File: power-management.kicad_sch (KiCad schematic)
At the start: 11 parts, among them Q3 DMP2070UQ-7, U2 AP2112K-3.3

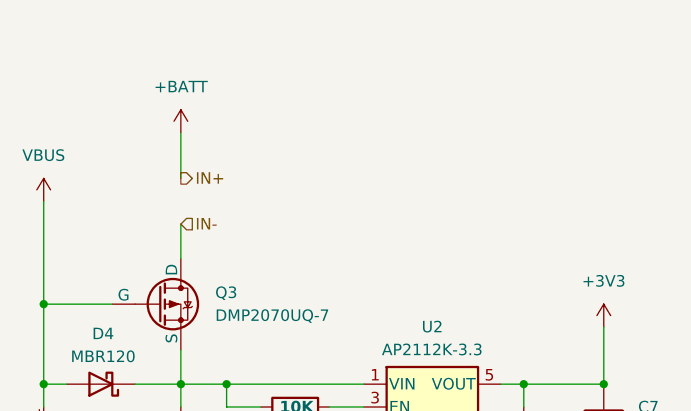
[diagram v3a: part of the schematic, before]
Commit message: Adding more 0 ohm resistors and pullups for I2C lines
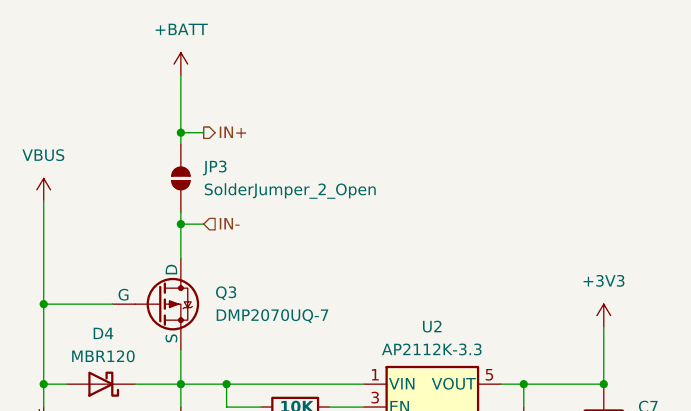
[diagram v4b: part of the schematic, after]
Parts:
- added JP3: SolderJumper_2_Open, Jumper:SolderJumper-2_P1.3mm_Open_TrianglePad1.0x1.5mm, symbol Jumper:SolderJumper_2_Open
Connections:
- net +BATT: now also JP3.2 (B)
- net IN-: now also JP3.1 (A)
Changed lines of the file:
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@@
+	)
+	(junction
+		(at 96.52 87.63)
+		(diameter 0)
+		(color 0 0 0 0)
 	)
 	(junction
@@
 	)
 	(junction
+		(at 96.52 77.47)
+		(diameter 0)
+		(color 0 0 0 0)
+	)
+	(junction
 		(at 134.62 105.41)
 		(diameter 0)
@@
 	(wire
 		(pts
+			(xy 96.52 86.36) (xy 96.52 87.63)
+		)
+		(stroke
+			(width 0)
+			(type default)
+		)
+	)
+	(wire
+		(pts
+			(xy 99.06 87.63) (xy 96.52 87.63)
+		)
+		(stroke
+			(width 0)
+			(type default)
+		)
+	)
+	(wire
+		(pts
 			(xy 143.51 113.03) (xy 143.51 115.57)
 		)
@@
 	(wire
 		(pts
-			(xy 96.52 77.47) (xy 96.52 82.55)
-		)
-		(stroke
-			(width 0)
-			(type default)
-		)
-	)
-	(wire
-		(pts
 			(xy 134.62 105.41) (xy 143.51 105.41)
 		)
@@
 	(wire
 		(pts
+			(xy 96.52 87.63) (xy 96.52 91.44)
+		)
+		(stroke
+			(width 0)
+			(type default)
+		)
+	)
+	(wire
+		(pts
 			(xy 91.44 105.41) (xy 96.52 105.41)
 		)
@@
 	(wire
 		(pts
+			(xy 99.06 77.47) (xy 96.52 77.47)
+		)
+		(stroke
+			(width 0)
+			(type default)
+		)
+	)
+	(wire
+		(pts
 			(xy 163.83 99.06) (xy 163.83 105.41)
 		)
@@
 	(wire
 		(pts
+			(xy 96.52 77.47) (xy 96.52 71.12)
+		)
+		(stroke
+			(width 0)
+			(type default)
+		)
+	)
+	(wire
+		(pts
 			(xy 113.03 107.95) (xy 116.84 107.95)
 		)
@@
 	(wire
 		(pts
+			(xy 96.52 77.47) (xy 96.52 78.74)
+		)
+		(stroke
+			(width 0)
+			(type default)
+		)
+	)
+	(wire
+		(pts
 			(xy 134.62 107.95) (xy 134.62 105.41)
-		)
-		(stroke
-			(width 0)
-			(type default)
-		)
-	)
-	(wire
-		(pts
-			(xy 96.52 87.63) (xy 96.52 91.44)
 		)
 		(stroke
@@
 	(hierarchical_label "IN+"
 		(shape output)
-		(at 96.52 82.55 0)
+		(at 99.06 77.47 0)
 		(fields_autoplaced yes)
 		(effects
@@
 	(hierarchical_label "IN-"
 		(shape input)
-		(at 96.52 87.63 0)
+		(at 99.06 87.63 0)
 		(fields_autoplaced yes)
 		(effects
@@
 	)
 	(symbol
+		(lib_id "Jumper:SolderJumper_2_Open")
+		(at 96.52 82.55 90)
+		(unit 1)
+		(exclude_from_sim yes)
+		(in_bom no)
+		(on_board yes)
+		(dnp no)
+		(property "Reference" "JP3"
+			(at 99.06 81.2799 90)
+			(effects
+				(font
+					(size 1.27 1.27)
+				)
+				(justify right)
+			)
+		)
+		(property "Value" "SolderJumper_2_Open"
+			(at 99.06 83.8199 90)
+			(effects
+				(font
+					(size 1.27 1.27)
+				)
+				(justify right)
+			)
+		)
+		(property "Footprint" "Jumper:SolderJumper-2_P1.3mm_Open_TrianglePad1.0x1.5mm"
+			(at 96.52 82.55 0)
+			(effects
+				(font
+					(size 1.27 1.27)
+				)
+				(hide yes)
+			)
+		)
+		(property "Datasheet" "~"
+			(at 96.52 82.55 0)
+			(effects
+				(font
+					(size 1.27 1.27)
+				)
+				(hide yes)
+			)
+		)
+		(property "Description" "Solder Jumper, 2-pole, open"
+			(at 96.52 82.55 0)
+			(effects
+				(font
+					(size 1.27 1.27)
+				)
+				(hide yes)
+			)
+		)
+		(property "Mfr" ""
+			(at 96.52 82.55 0)
+			(effects
+				(font
+					(size 1.27 1.27)
+				)
+				(hide yes)
+			)
+		)
+		(property "Mfr P/N" ""
+			(at 96.52 82.55 0)
+			(effects
+				(font
+					(size 1.27 1.27)
+				)
+				(hide yes)
+			)
+		)
+		(property "Supplier_1" ""
+			(at 96.52 82.55 0)
+			(effects
+				(font
+					(size 1.27 1.27)
+				)
+				(hide yes)
+			)
+		)
+		(property "Supplier_1 P/N" ""
+			(at 96.52 82.55 0)
+			(effects
+				(font
+					(size 1.27 1.27)
+				)
+				(hide yes)
+			)
+		)
+		(property "Supplier_1 Unit Price" ""
+			(at 96.52 82.55 0)
+			(effects
+				(font
+					(size 1.27 1.27)
+				)
+				(hide yes)
+			)
+		)
+		(property "Supplier_1 Price @ Qty" ""
+			(at 96.52 82.55 0)
+			(effects
+				(font
+					(size 1.27 1.27)
+				)
+				(hide yes)
+			)
+		)
+		(property "Supplier_2" ""
+			(at 96.52 82.55 0)
+			(effects
+				(font
+					(size 1.27 1.27)
+				)
+				(hide yes)
+			)
+		)
+		(property "Supplier_2 P/N" ""
+			(at 96.52 82.55 0)
+			(effects
+				(font
+					(size 1.27 1.27)
+				)
+				(hide yes)
+			)
+		)
+		(property "Supplier_2 Unit Price" ""
+			(at 96.52 82.55 0)
+			(effects
+				(font
+					(size 1.27 1.27)
+				)
+				(hide yes)
+			)
+		)
+		(property "Supplier_2 Price @ Qty" ""
+			(at 96.52 82.55 0)
+			(effects
+				(font
+					(size 1.27 1.27)
+				)
+				(hide yes)
+			)
+		)
+		(pin "1"
+		)
+		(pin "2"
+		)
+		(instances
+			(project "roamer"
+				(path "/1c59de6a-87fe-4223-8898-4b0383164a31/f8947920-db82-4e9f-9d4f-25a180fcfca7"
+					(reference "JP3")
+					(unit 1)
+				)
+			)
+		)
+	)
+	(symbol
 		(lib_id "power:+BATT")
-		(at 96.52 77.47 0)
+		(at 96.52 71.12 0)
 		(unit 1)
 		(exclude_from_sim no)
@@
 		(fields_autoplaced yes)
 		(property "Reference" "#PWR020"
-			(at 96.52 81.28 0)
+			(at 96.52 74.93 0)
 			(effects
 				(font
@@
 		)
 		(property "Value" "+BATT"
-			(at 96.52 72.39 0)
+			(at 96.52 66.04 0)
 			(effects
 				(font
@@
 		)
 		(property "Footprint" ""
-			(at 96.52 77.47 0)
+			(at 96.52 71.12 0)
 			(effects
 				(font
@@
 		)
 		(property "Datasheet" ""
-			(at 96.52 77.47 0)
+			(at 96.52 71.12 0)
 			(effects
 				(font
@@
 		)
 		(property "Description" "Power symbol creates a global label with name \"+BATT\""
-			(at 96.52 77.47 0)
-			(effects
-				(font
+			(at 96.52 71.12 0)
+			(effects
+				(font

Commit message: Adding testpoints to I2C, SPI, and signals
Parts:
- added TP7: TestPoint, TestPoint:TestPoint_Loop_D2.50mm_Drill1.0mm, symbol Connector:TestPoint
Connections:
- net +3V3: now also TP7.1
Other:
- moved on the sheet: C10, C11, C5

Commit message: Fixing lots of ERC errors
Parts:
- removed R9: 100K, Resistor_SMD:R_Array_Convex_4x1206, symbol Device:R_Network04_Split
- added R9: 100K, Resistor_THT:R_Array_SIP8, symbol Device:R_Pack04_SIP_Split
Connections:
- net GND: now also R9.5 (R3.1)
- net VBUS: now also R9.6 (R3.2)
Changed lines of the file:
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@@
+	)
+	(junction
+		(at 109.22 105.41)
+		(diameter 0)
+		(color 0 0 0 0)
 	)
 	(junction
@@
 	(wire
 		(pts
-			(xy 101.6 105.41) (xy 116.84 105.41)
+			(xy 101.6 105.41) (xy 109.22 105.41)
 		)
 		(stroke
@@
 		(pts
 			(xy 96.52 105.41) (xy 96.52 107.95)
+		)
+		(stroke
+			(width 0)
+			(type default)
+		)
+	)
+	(wire
+		(pts
+			(xy 109.22 105.41) (xy 116.84 105.41)
 		)
 		(stroke
@@
 	)
 	(symbol
+		(lib_id "power:PWR_FLAG")
+		(at 109.22 105.41 0)
+		(unit 1)
+		(exclude_from_sim no)
+		(in_bom yes)
+		(on_board yes)
+		(dnp no)
+		(property "Reference" "#FLG05"
+			(at 109.22 103.505 0)
+			(effects
+				(font
+					(size 1.27 1.27)
+				)
+				(hide yes)
+			)
+		)
+		(property "Value" "PWR_FLAG"
+			(at 109.474 101.854 0)
+			(effects
+				(font
+					(size 1.27 1.27)
+				)
+			)
+		)
+		(property "Footprint" ""
+			(at 109.22 105.41 0)
+			(effects
+				(font
+					(size 1.27 1.27)
+				)
+				(hide yes)
+			)
+		)
+		(property "Datasheet" "~"
+			(at 109.22 105.41 0)
+			(effects
+				(font
+					(size 1.27 1.27)
+				)
+				(hide yes)
+			)
+		)
+		(property "Description" "Special symbol for telling ERC where power comes from"
+			(at 109.22 105.41 0)
+			(effects
+				(font
+					(size 1.27 1.27)
+				)
+				(hide yes)
+			)
+		)
+		(pin "1"
+		)
+		(instances
+			(project ""
+				(path "/1c59de6a-87fe-4223-8898-4b0383164a31/f8947920-db82-4e9f-9d4f-25a180fcfca7"
+					(reference "#FLG05")
+					(unit 1)
+				)
+			)
+		)
+	)
+	(symbol
 		(lib_id "Device:C")
 		(at 143.51 109.22 0)
@@
 					(reference "C7")
 					(unit 1)
-				)
-			)
-		)
-	)
-	(symbol
-		(lib_id "Device:R_Network04_Split")
-		(at 81.28 111.76 0)
-		(unit 3)
-		(exclude_from_sim no)
-		(in_bom yes)
-		(on_board yes)
-		(dnp no)
-		(property "Reference" "R9"
-			(at 83.82 110.4899 0)
-			(effects
-				(font
-					(size 1.27 1.27)
-				)
-				(justify left)
-			)
-		)
-		(property "Value" "100K"
-			(at 81.534 114.3 90)
-			(effects
-				(font
-					(size 1.27 1.27)
-					(thickness 0.254)
-					(bold yes)
-				)
-				(justify left)
-			)
-		)
-		(property "Footprint" "Resistor_SMD:R_Array_Convex_4x1206"
-			(at 79.248 111.76 90)
-			(effects
-				(font
-					(size 1.27 1.27)
-				)
-				(hide yes)
-			)
-		)
-		(property "Datasheet" "https://www.bourns.com/docs/Product-Datasheets/CATCAY.pdf"
-			(at 81.28 111.76 0)
-			(effects
-				(font
-					(size 1.27 1.27)
-				)
-				(hide yes)
-			)
-		)
-		(property "Description" "100k Ohm 1% 62.5mW Power Per Element Isolated 4 Resistor Network/Array 200pm/°C 1206 (3216 Metric), Convex, Long Side Terminals."
-			(at 81.28 111.76 0)
-			(effects
-				(font
-					(size 1.27 1.27)
-				)
-				(hide yes)
-			)
-		)
-		(property "Mfr" "Bourns Inc."
-			(at 81.28 111.76 0)
-			(effects
-				(font
-					(size 1.27 1.27)
-				)
-				(hide yes)
-			)
-		)
-		(property "Mfr P/N" "CAY16-1003F4LF"
-			(at 81.28 111.76 0)
-			(effects
-				(font
-					(size 1.27 1.27)
-				)
-				(hide yes)
-			)
-		)
-		(property "Supplier_1" "Digikey"
-			(at 81.28 111.76 0)
-			(effects
-				(font
-					(size 1.27 1.27)
-				)
-				(hide yes)
-			)
-		)
-		(property "Supplier_1 P/N" "CAY16-1003F4LFCT-ND"
-			(at 81.28 111.76 0)
-			(effects
-				(font
-					(size 1.27 1.27)
-				)
-				(hide yes)
-			)
-		)
-		(property "Supplier_1 Unit Price" "0.10"
-			(at 81.28 111.76 0)
-			(effects
-				(font
-					(size 1.27 1.27)
-				)
-				(hide yes)
-			)
-		)
-		(property "Supplier_1 Price @ Qty" "0.03170"
-			(at 81.28 111.76 0)
-			(effects
-				(font
-					(size 1.27 1.27)
-				)
-				(hide yes)
-			)
-		)
-		(property "Supplier_2" ""
-			(at 81.28 111.76 0)
-			(effects
-				(font
-					(size 1.27 1.27)
-				)
-				(hide yes)
-			)
-		)
-		(property "Supplier_2 P/N" ""
-			(at 81.28 111.76 0)
-			(effects
-				(font
-					(size 1.27 1.27)
-				)
-				(hide yes)
-			)
-		)
-		(property "Supplier_2 Unit Price" ""
-			(at 81.28 111.76 0)
-			(effects
-				(font
-					(size 1.27 1.27)
-				)
-				(hide yes)
-			)
-		)
-		(property "Supplier_2 Price @ Qty" ""
-			(at 81.28 111.76 0)
-			(effects
-				(font
-					(size 1.27 1.27)
-				)
-				(hide yes)
-			)
-		)
-		(pin "2"
-		)
-		(pin "3"
-		)
-		(pin "4"
-		)
-		(pin "5"
-		)
-		(pin "1"
-		)
-		(instances
-			(project "roamer"
-				(path "/1c59de6a-87fe-4223-8898-4b0383164a31/f8947920-db82-4e9f-9d4f-25a180fcfca7"
-					(reference "R9")
-					(unit 3)
 				)
 			)
@@
 				)
 			)
+		)
+	)
+	(symbol
+		(lib_id "Device:R_Pack04_SIP_Split")
+		(at 81.28 111.76 0)
+		(unit 3)
+		(exclude_from_sim no)
+		(in_bom yes)
+		(on_board yes)
+		(dnp no)
+		(property "Reference" "R9"
+			(at 83.82 110.4899 0)
+			(effects
+				(font
+					(size 1.27 1.27)
+				)
+				(justify left)
+			)
+		)
+		(property "Value" "100K"
+			(at 81.28 114.554 90)
+			(effects
+				(font
+					(size 1.27 1.27)
+					(thickness 0.254)
+					(bold yes)
+				)
+				(justify left)
+			)
+		)
+		(property "Footprint" "Resistor_THT:R_Array_SIP8"
+			(at 79.248 111.76 90)
+			(effects
+				(font
+					(size 1.27 1.27)
+				)
+				(hide yes)
+			)
+		)
+		(property "Datasheet" "https://www.bourns.com/docs/Product-Datasheets/CATCAY.pdf"
+			(at 81.28 111.76 0)
+			(effects
+				(font
+					(size 1.27 1.27)
+				)
+				(hide yes)
+			)
+		)
+		(property "Description" "4 resistor network, parallel topology, SIP package, split"
+			(at 81.28 111.76 0)
+			(effects
+				(font
+					(size 1.27 1.27)
+				)
+				(hide yes)
+			)
+		)
+		(property "Mfr" "Bourns Inc."
+			(at 81.28 111.76 0)
+			(effects
+				(font
+					(size 1.27 1.27)
+				)
+				(hide yes)
+			)
+		)
+		(property "Mfr P/N" "CAY16-1003F4LF"
+			(at 81.28 111.76 0)
+			(effects
+				(font
+					(size 1.27 1.27)
+				)
+				(hide yes)
+			)
+		)
+		(property "Supplier_1" "Digikey"
+			(at 81.28 111.76 0)
+			(effects
+				(font
+					(size 1.27 1.27)
+				)
+				(hide yes)
+			)
+		)
+		(property "Supplier_1 P/N" "CAY16-1003F4LFCT-ND"
+			(at 81.28 111.76 0)
+			(effects
+				(font
+					(size 1.27 1.27)
+				)
+				(hide yes)
+			)
+		)
+		(property "Supplier_1 Unit Price" "0.10"
+			(at 81.28 111.76 0)
+			(effects
+				(font
+					(size 1.27 1.27)
+				)
+				(hide yes)
+			)
+		)
+		(property "Supplier_1 Price @ Qty" "0.03170"
+			(at 81.28 111.76 0)
+			(effects
+				(font
+					(size 1.27 1.27)
+				)
+				(hide yes)
+			)
+		)
+		(property "Supplier_2" ""
+			(at 81.28 111.76 0)
+			(effects
+				(font
+					(size 1.27 1.27)
+				)
+				(hide yes)
+			)
+		)
+		(property "Supplier_2 P/N" ""
+			(at 81.28 111.76 0)
+			(effects
+				(font
+					(size 1.27 1.27)
+				)
+				(hide yes)
+			)
+		)
+		(property "Supplier_2 Unit Price" ""
+			(at 81.28 111.76 0)
+			(effects
+				(font
+					(size 1.27 1.27)
+				)
+				(hide yes)
+			)
+		)
+		(property "Supplier_2 Price @ Qty" ""
+			(at 81.28 111.76 0)
+			(effects
+				(font
+					(size 1.27 1.27)
+				)
+				(hide yes)
+			)
+		)
+		(pin "7"
+		)
+		(pin "2"
+		)
+		(pin "3"
+		)
+		(pin "4"
+		)
+		(pin "6"
+		)
+		(pin "8"
+		)
+		(pin "5"
+		)
+		(pin "1"
+		)
+		(instances
+			(project "roamer"
+				(path "/1c59de6a-87fe-4223-8898-4b0383164a31/f8947920-db82-4e9f-9d4f-25a180fcfca7"
+					(reference "R9")
+					(unit 3)
+				)
+			)

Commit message: Starting layout
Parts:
- R9: footprint Resistor_THT:R_Array_SIP8 -> Resistor_SMD:R_Array_Convex_4x1206
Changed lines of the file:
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@@
 			)
 		)
-		(property "Footprint" "Resistor_THT:R_Array_SIP8"
+		(property "Footprint" "Resistor_SMD:R_Array_Convex_4x1206"
 			(at 79.248 111.76 90)
 			(effects

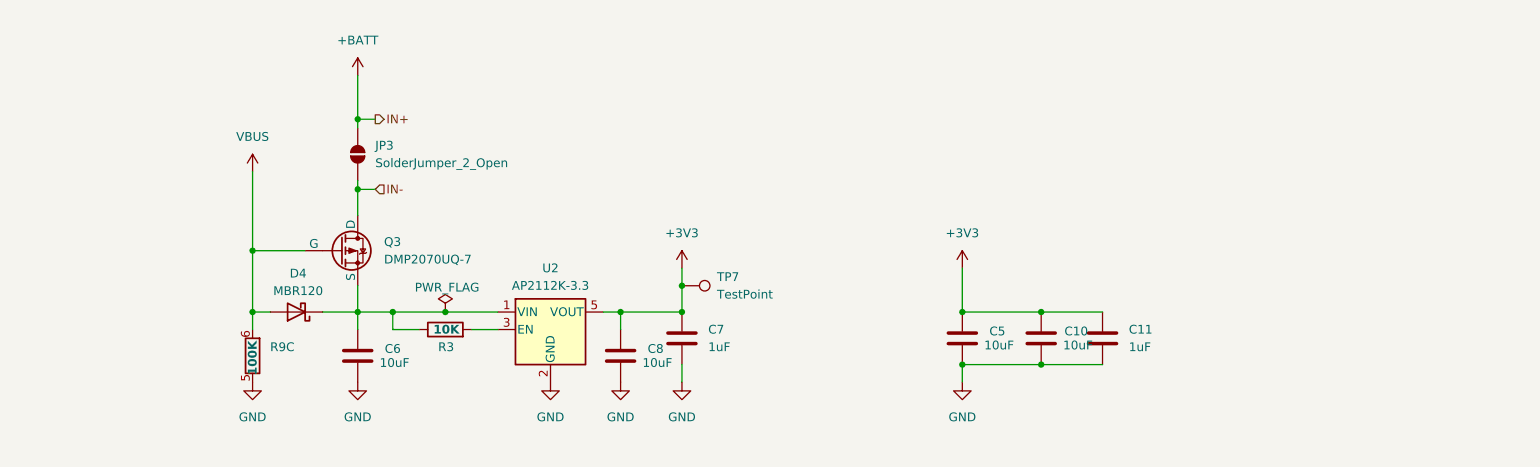
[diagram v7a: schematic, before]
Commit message: Adding 5V boost
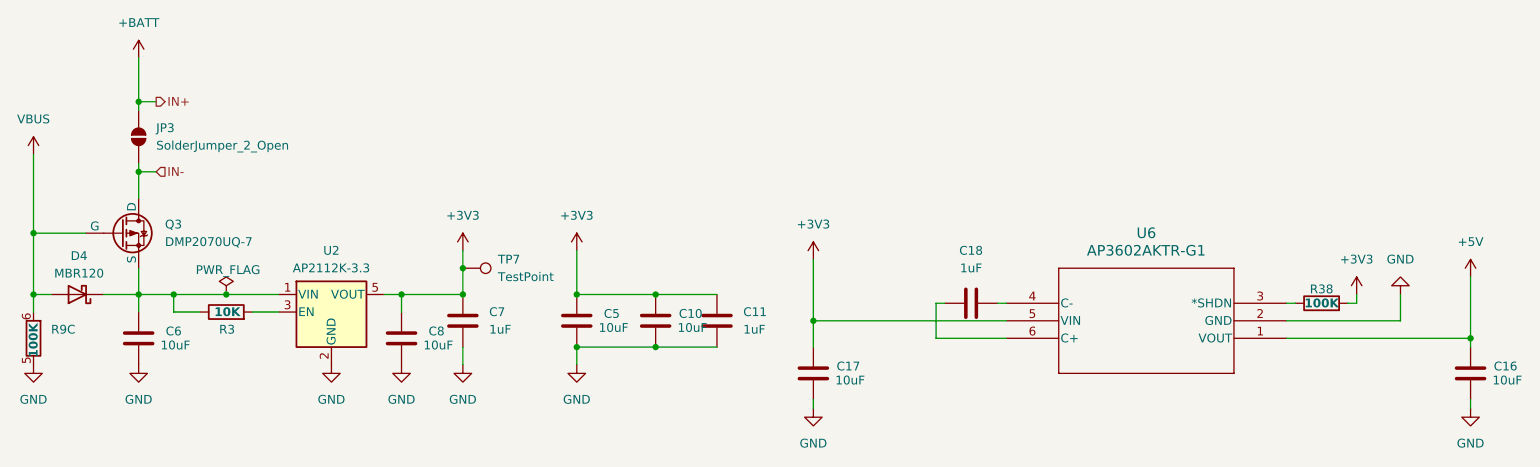
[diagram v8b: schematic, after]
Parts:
- added C16, C17: 10uF, Inductor_SMD:L_0805_2012Metric, symbol Device:C
- added C18: 1uF, Capacitor_SMD:C_0603_1608Metric, symbol Device:C
- added R38: 100K, symbol Device:R
- added U6: AP3602AKTR-G1, footprints:SOT-23-6_DIO, symbol _AP3602:AP3602AKTR-G1
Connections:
- net +3V3: now also C17.1, R38.2, U6.5 (VIN)
- net GND: now also C16.2, C17.2, U6.2 (GND)
- new net: R38.1, U6.3 (*SHDN)
- new net: C18.1, U6.4 (C-)
- new net: C18.2, U6.6 (C+)
- new net +5V: C16.1, U6.1 (VOUT)
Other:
- moved on the sheet: C10, C11, C5, C6, C7, C8, D4, JP3, Q3, R3, R9C, TP7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
